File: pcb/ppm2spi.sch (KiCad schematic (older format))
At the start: 40 parts, among them IC1 ATMEGA328-A, K1 CONN_3, P1 CONN_5, P2 CONN_6, P3 CONN_3X2, P4 CONN_9, P5 CONN_2, SW1 SW_PUSH, U1 MCP1702-5v, U2 MCP1702-3.3v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

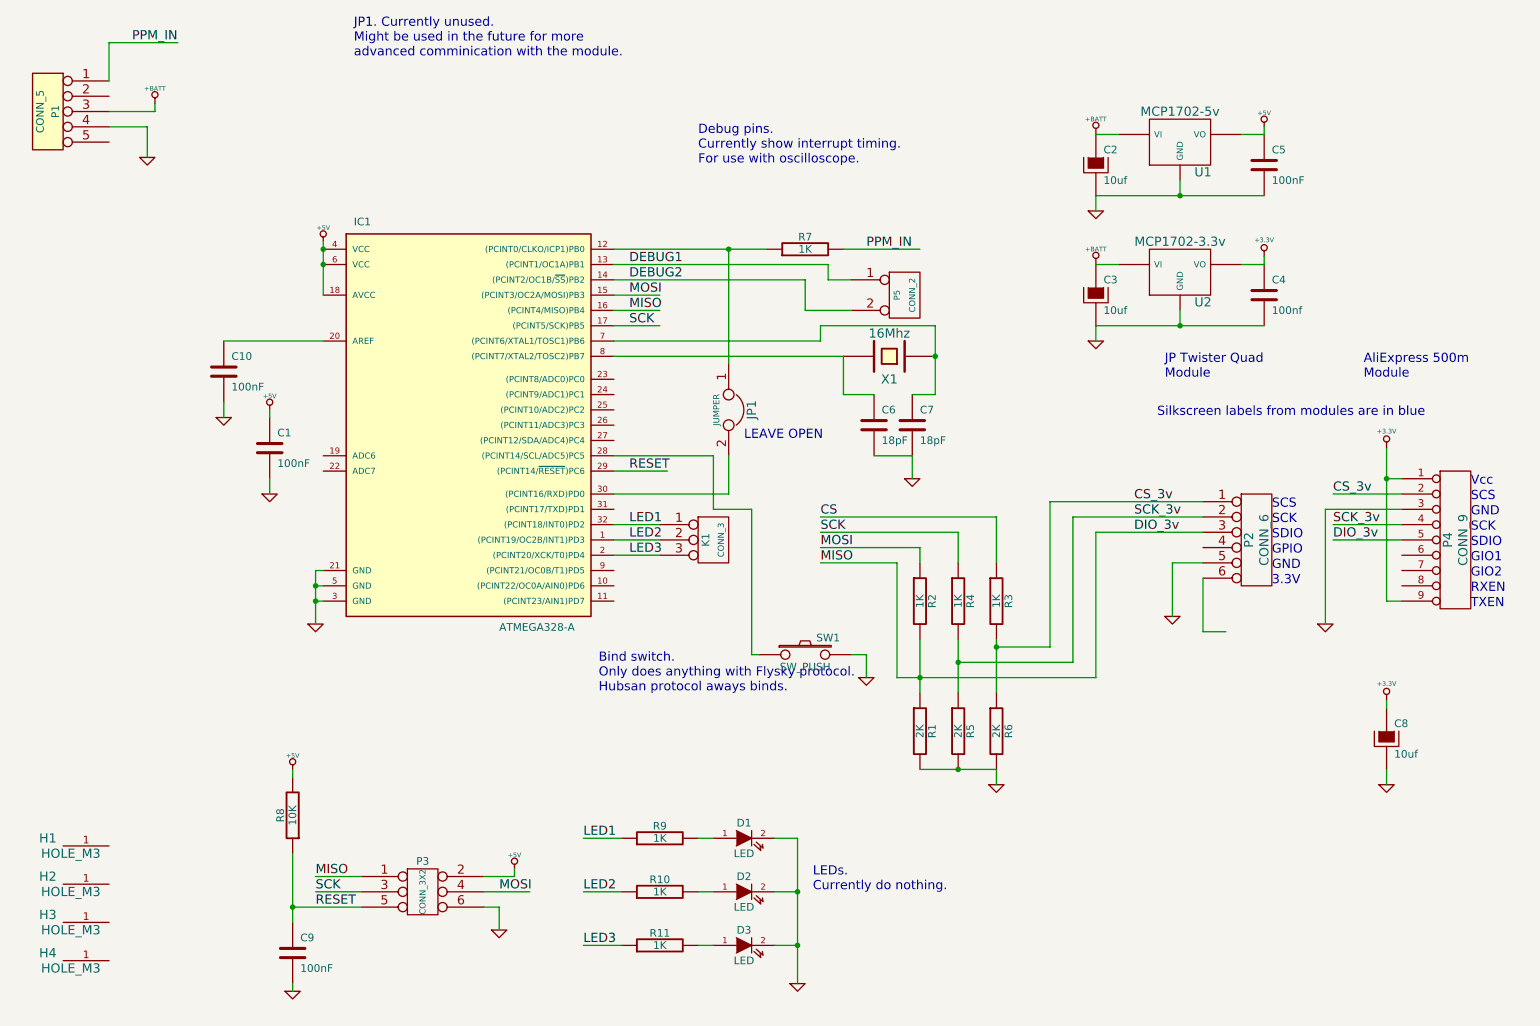
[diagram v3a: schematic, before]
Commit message: It works... but be careful the various mods on the Flysky protocol can cause unexpected motor starts if you get the wrong one. Ask me how I found out :) see flysky_a7105.c line 172 for more details. As you will see a couple of the options toggle bits in the throttle channel.
Also added another LED to show when binding is taking place and finished.

Next the PCB layout.
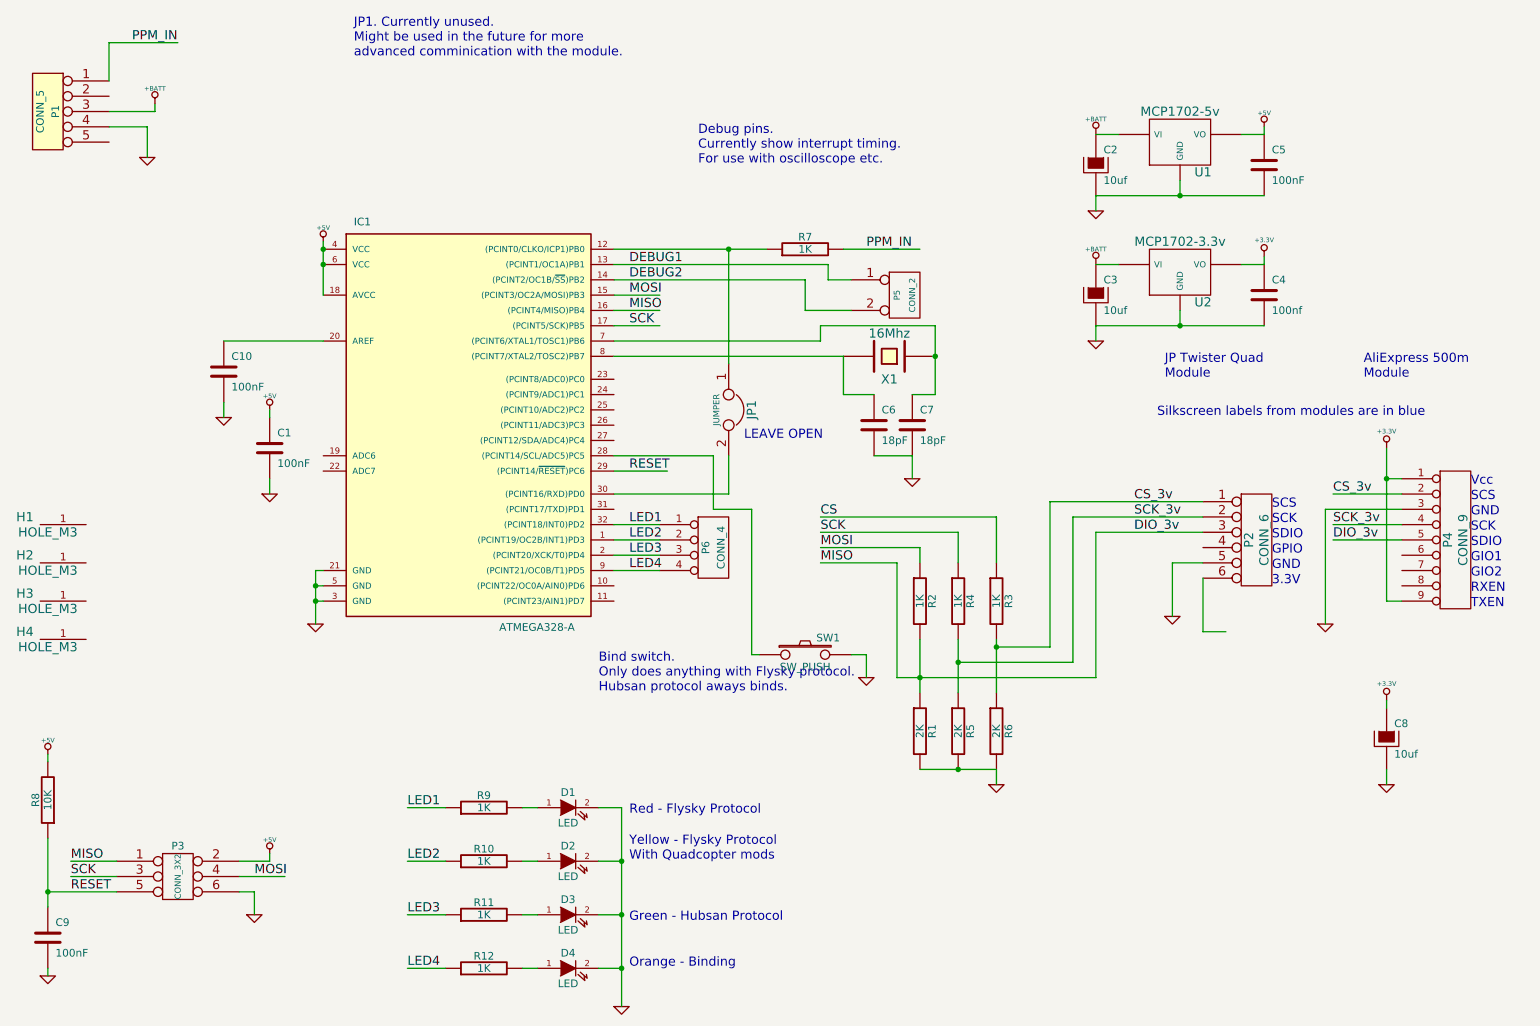
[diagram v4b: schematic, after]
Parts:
- removed K1: CONN_3, symbol CONN_3
- added D4: LED, symbol LED
- added P6: CONN_4, symbol CONN_4
- added R12: 1K, symbol R
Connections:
- net labels added: LED4
- wire segments 119 -> 123
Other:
- note added: "Debug pins.\nCurrently show interrupt timing.\nFor use with oscilloscope etc."
- note added: "Green - Hubsan Protocol"
- note added: "Orange - Binding"
- note added: "Red - Flysky Protocol"
- note added: "Yellow - Flysky Protocol\nWith Quadcopter mods"
- note removed: "Debug pins.\nCurrently show interrupt timing.\nFor use with oscilloscope."
- note removed: "LEDs.\nCurrently do nothing."
- moved on the sheet: C9, D1, D2, D3, H1, H2, H3, H4, P3, R10, R11, R8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

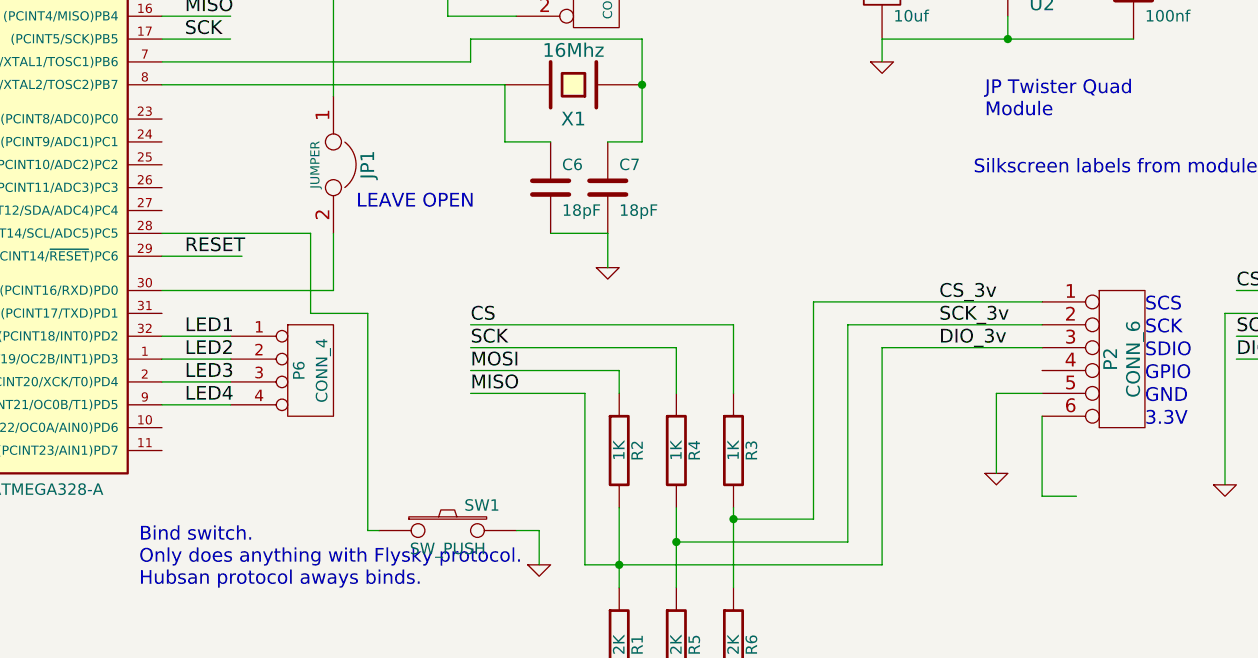
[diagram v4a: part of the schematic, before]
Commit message: PCB update. Needs silkscreen labels sorting.
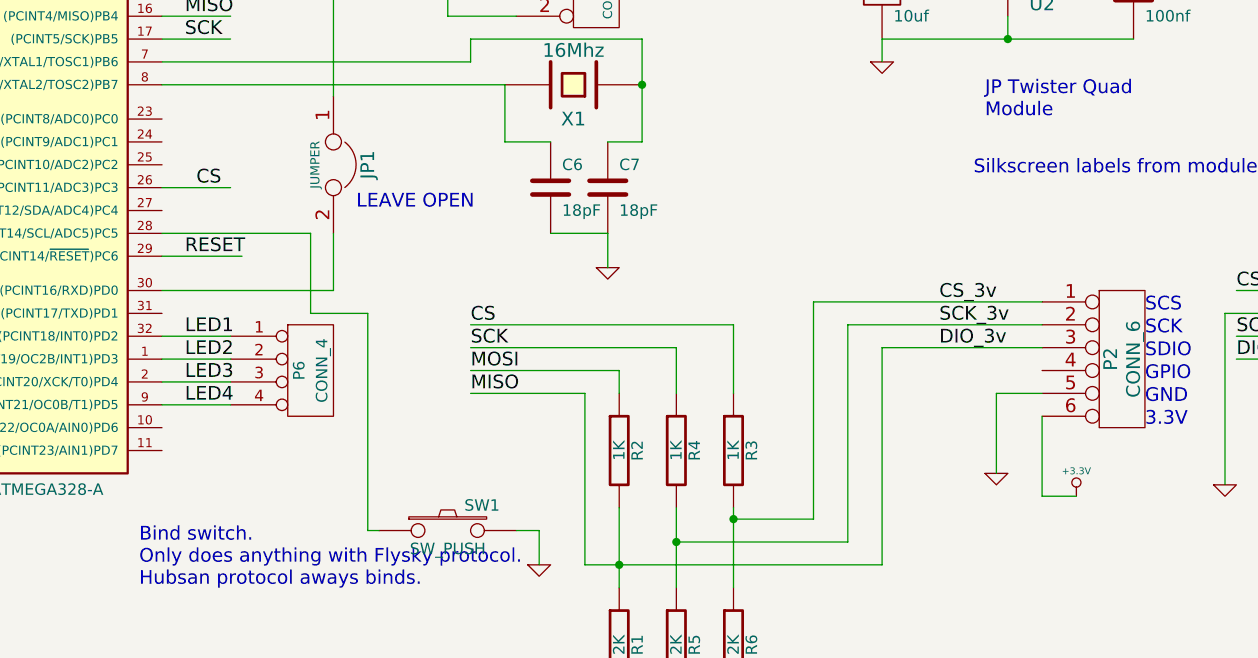
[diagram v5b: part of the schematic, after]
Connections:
- wire segments 123 -> 124
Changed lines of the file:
@@
-EESchema Schematic File Version 2  date 06/05/2013 12:51:55
+EESchema Schematic File Version 2  date 06/05/2013 18:39:08
 LIBS:power
 LIBS:device
@@
 Wire Wire Line
 	4900 4400 5200 4400
+Text Label 5050 3450 0    60   ~ 0
+CS
+Wire Wire Line
+	4900 3450 5200 3450
+$Comp
+L +3.3V #PWR?
+U 1 1 5187EC96
+P 8900 4800
+F 0 "#PWR?" H 8900 4760 30  0001 C CNN
+F 1 "+3.3V" H 8900 4910 30  0000 C CNN
+F 2 "" H 8900 4800 60  0001 C CNN
+F 3 "" H 8900 4800 60  0001 C CNN
+	1    8900 4800
+	1    0    0    -1
+$EndComp
 $EndSCHEMATC

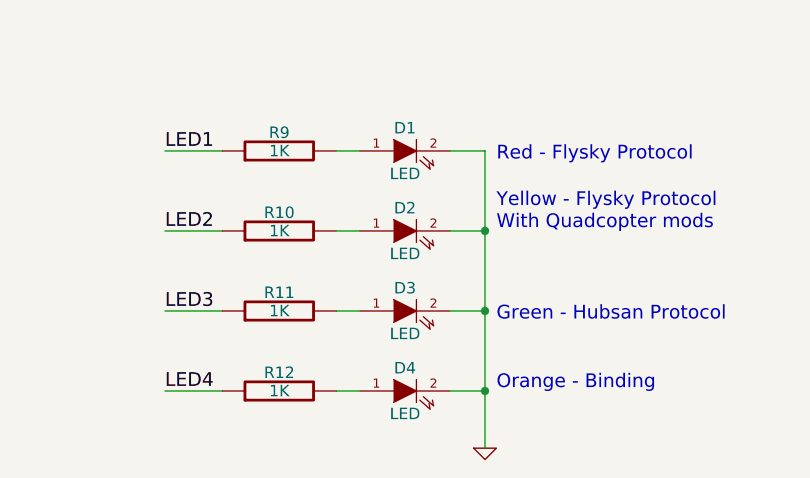
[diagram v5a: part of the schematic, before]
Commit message: Closer with the PCB. Last step a bigger 3.3v reg.
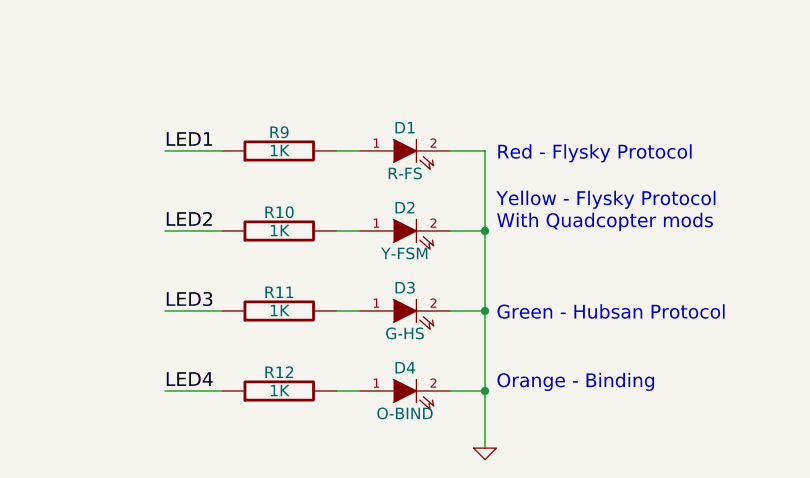
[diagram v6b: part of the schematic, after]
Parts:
- D1: value LED -> R-FS
- D2: value LED -> Y-FSM
- D3: value LED -> G-HS
- D4: value LED -> O-BIND
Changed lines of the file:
@@
-EESchema Schematic File Version 2  date 06/05/2013 18:39:08
+EESchema Schematic File Version 2  date 06/05/2013 21:01:11
 LIBS:power
 LIBS:device
@@
 P 4600 6650
 F 0 "D3" H 4600 6750 50  0000 C CNN
-F 1 "LED" H 4600 6550 50  0000 C CNN
+F 1 "G-HS" H 4600 6550 50  0000 C CNN
 F 2 "" H 4600 6650 60  0001 C CNN
 F 3 "" H 4600 6650 60  0001 C CNN
@@
 P 4600 6300
 F 0 "D2" H 4600 6400 50  0000 C CNN
-F 1 "LED" H 4600 6200 50  0000 C CNN
+F 1 "Y-FSM" H 4600 6200 50  0000 C CNN
 F 2 "" H 4600 6300 60  0001 C CNN
 F 3 "" H 4600 6300 60  0001 C CNN
@@
 P 4600 5950
 F 0 "D1" H 4600 6050 50  0000 C CNN
-F 1 "LED" H 4600 5850 50  0000 C CNN
+F 1 "R-FS" H 4600 5850 50  0000 C CNN
 F 2 "" H 4600 5950 60  0001 C CNN
 F 3 "" H 4600 5950 60  0001 C CNN
@@
 P 4600 7000
 F 0 "D4" H 4600 7100 50  0000 C CNN
-F 1 "LED" H 4600 6900 50  0000 C CNN
+F 1 "O-BIND" H 4600 6900 50  0000 C CNN
 F 2 "" H 4600 7000 60  0001 C CNN
 F 3 "" H 4600 7000 60  0001 C CNN

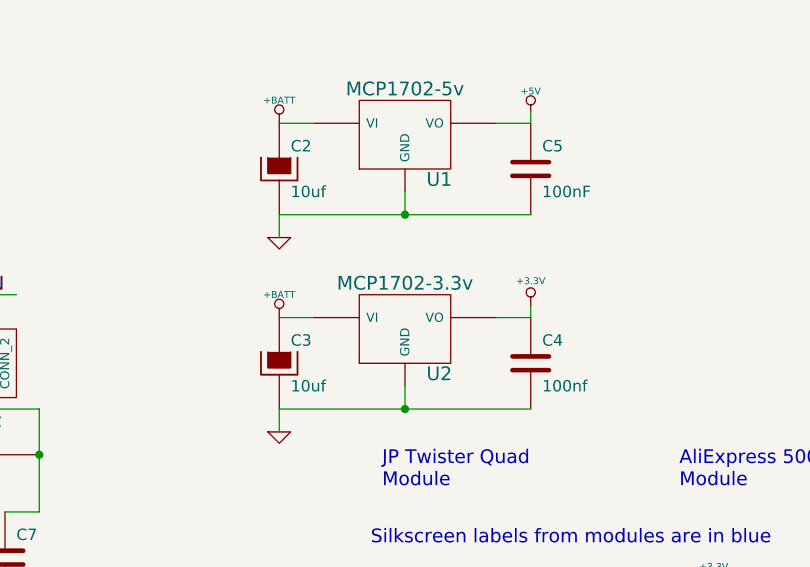
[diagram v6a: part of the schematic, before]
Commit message: Bigger 3.3v reg. Think that's it done !
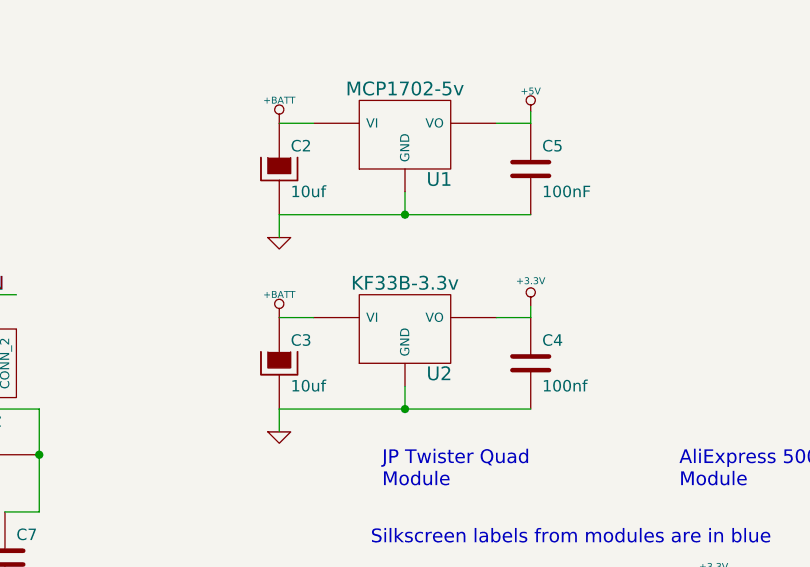
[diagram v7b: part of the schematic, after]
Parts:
- U2: value MCP1702-3.3v -> KF33B-3.3v
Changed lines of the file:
@@
-EESchema Schematic File Version 2  date 06/05/2013 21:01:11
+EESchema Schematic File Version 2  date 06/05/2013 21:20:18
 LIBS:power
 LIBS:device
@@
 P 8600 2450
 F 0 "U2" H 8750 2254 60  0000 C CNN
-F 1 "MCP1702-3.3v" H 8600 2650 60  0000 C CNN
+F 1 "KF33B-3.3v" H 8600 2650 60  0000 C CNN
 F 2 "" H 8600 2450 60  0001 C CNN
 F 3 "" H 8600 2450 60  0001 C CNN

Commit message: More PCB updates and some feature creep.
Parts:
- added JP2: JUMPER, ~, symbol JUMPER
- added K1: CONN_3, symbol CONN_3
- added P7: CONN_2, symbol CONN_2
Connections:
- net labels added: BIND, CH_ORD, Rx, Tx
- wire segments 124 -> 132
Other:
- note added: "Alternative channel order"
- note added: "Alternative channel order\nAllows this module to work\nwith other transmitters"
- note added: "Bind"
- note added: "Bind switch.\nOnly does anything with Flysky protocol.\nHubsan protocol always binds."
- note added: "Serial comms breakout"
- note removed: "Bind switch.\nOnly does anything with Flysky protocol.\nHubsan protocol aways binds."
- moved on the sheet: C6, C7, C8, JP1, P2, P4, P5, R1, R2, R3, R4, R5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
